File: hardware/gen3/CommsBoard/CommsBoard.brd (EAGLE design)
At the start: 140 x 107 mm, 41 parts, among them U1 ATMEGA165PV-8AU

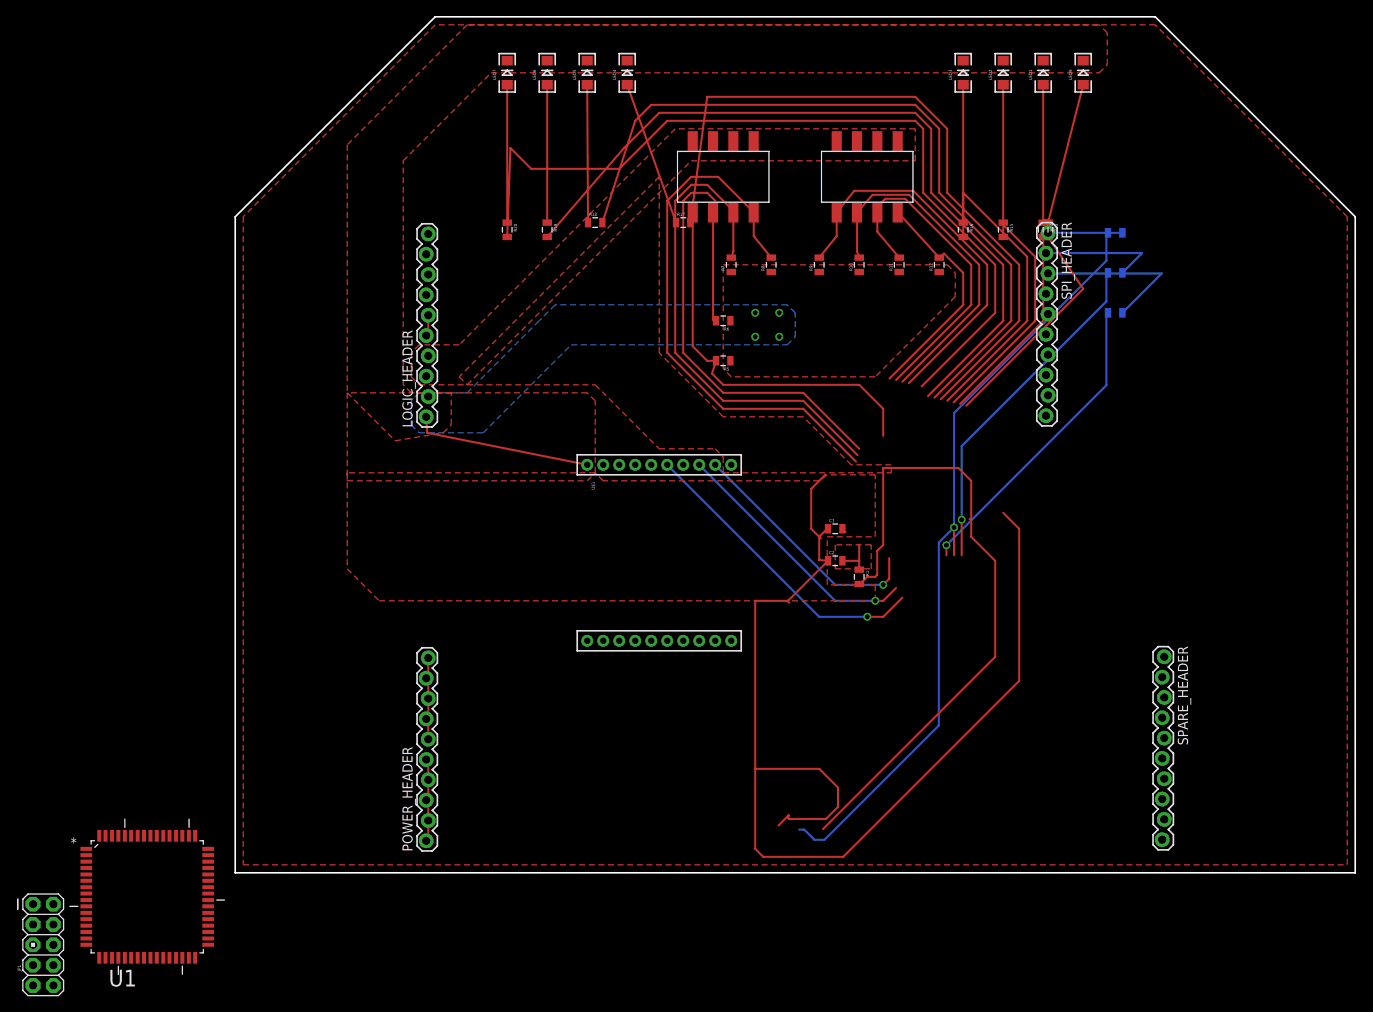
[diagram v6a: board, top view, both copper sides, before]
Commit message: new dimensions for boards
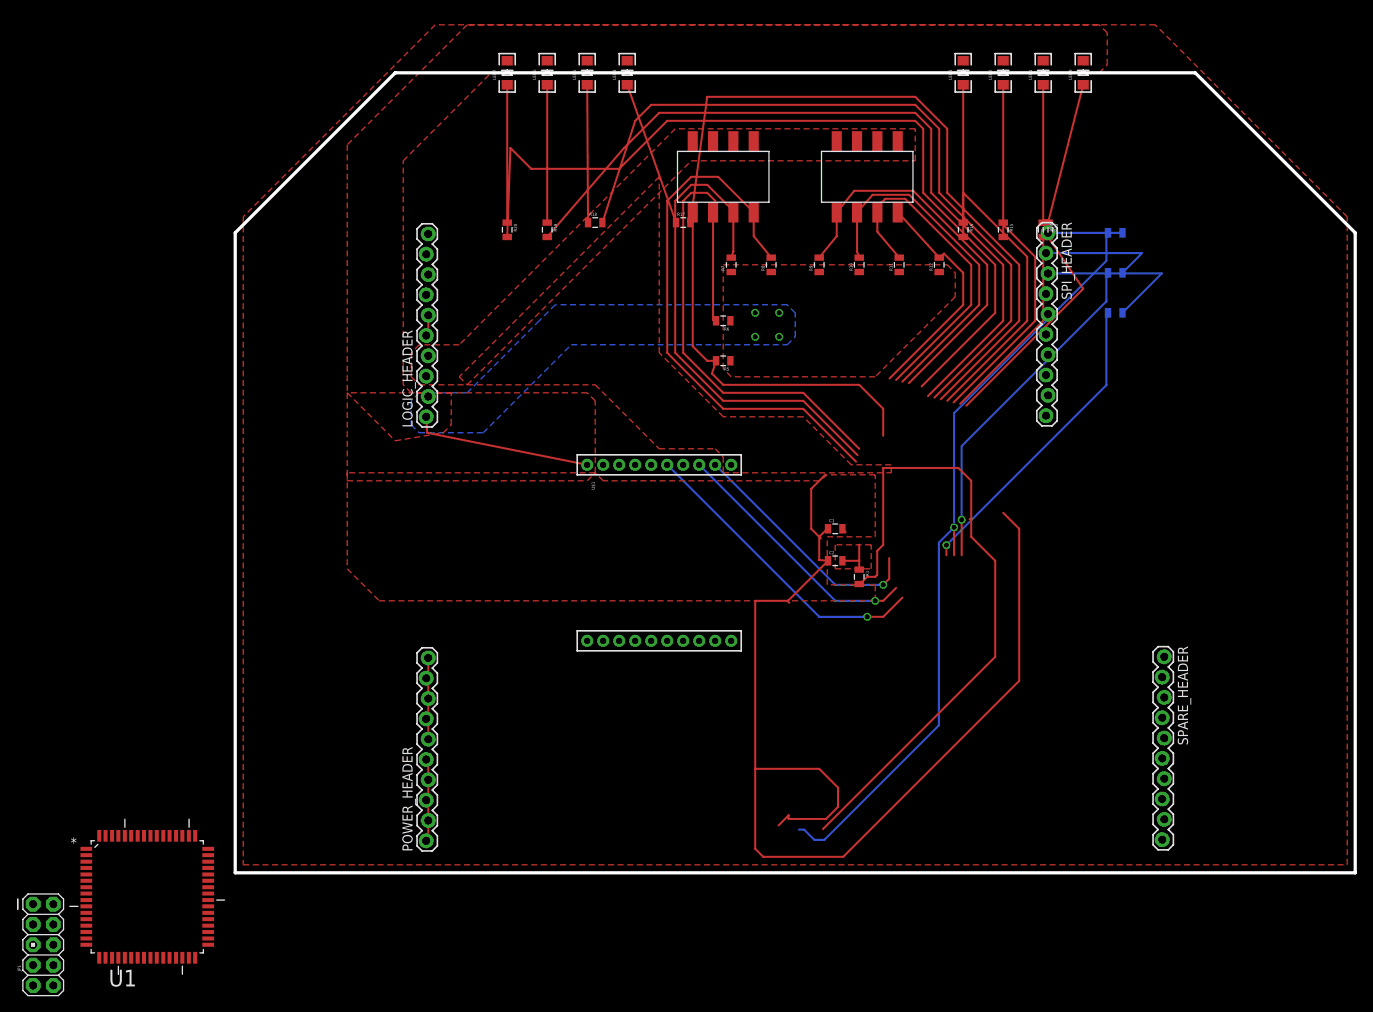
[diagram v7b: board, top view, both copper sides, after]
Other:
- board size 140 x 107 mm -> 140 x 100 mm
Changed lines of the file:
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@@
 <?xml version="1.0" encoding="utf-8"?>
 <!DOCTYPE eagle SYSTEM "eagle.dtd">
-<eagle version="7.2.0">
+<eagle version="6.4">
 <drawing>
 <settings>
@@
 <setting verticaltext="up"/>
 </settings>
-<grid distance="0.05" unitdist="inch" unit="inch" style="lines" multiple="1" display="yes" altdistance="0.01" altunitdist="mm" altunit="mm"/>
+<grid distance="1" unitdist="mm" unit="mm" style="lines" multiple="1" display="yes" altdistance="0.01" altunitdist="mm" altunit="mm"/>
 <layers>
 <layer number="1" name="Top" color="4" fill="1" visible="yes" active="yes"/>
@@
 <board>
 <plain>
-<wire x1="0" y1="0" x2="0" y2="82" width="0.2032" layer="20"/>
-<wire x1="0" y1="82" x2="25" y2="107" width="0.2032" layer="20"/>
-<wire x1="25" y1="107" x2="115" y2="107" width="0.2032" layer="20"/>
-<wire x1="115" y1="107" x2="140" y2="82" width="0.2032" layer="20"/>
-<wire x1="140" y1="82" x2="140" y2="0" width="0.2032" layer="20"/>
-<wire x1="140" y1="0" x2="0" y2="0" width="0.2032" layer="20"/>
-<wire x1="70" y1="107" x2="70" y2="0" width="0.4064" layer="23"/>
-<wire x1="120" y1="107" x2="120" y2="0" width="0.4064" layer="23"/>
-<wire x1="20" y1="0" x2="20" y2="107" width="0.4064" layer="23"/>
-<wire x1="-1" y1="82" x2="142" y2="82" width="0.4064" layer="23"/>
+<wire x1="0" y1="0" x2="0" y2="80" width="0.4064" layer="20"/>
+<wire x1="0" y1="80" x2="20" y2="100" width="0.4064" layer="20"/>
+<wire x1="20" y1="100" x2="120" y2="100" width="0.4064" layer="20"/>
+<wire x1="120" y1="100" x2="140" y2="80" width="0.4064" layer="20"/>
+<wire x1="140" y1="80" x2="140" y2="0" width="0.4064" layer="20"/>
+<wire x1="140" y1="0" x2="0" y2="0" width="0.4064" layer="20"/>
 </plain>
 <attributes>
@@
 <pass name="Default">
 <param name="RoutingGrid" value="12.5mil"/>
-<param name="AutoGrid" value="1"/>
-<param name="Efforts" value="0"/>
-<param name="TopRouterVariant" value="1"/>
 <param name="tpViaShape" value="round"/>
 <param name="PrefDir.1" value="*"/>

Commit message: headers placed
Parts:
- moved LOGIC_HEADER 40.0 mm to (23.0, 97.0), turned to 0 degrees
- moved SPARE_HEADER 32.6 mm to (94.0, 3.00), turned to 0 degrees
- moved SPI_HEADER 18.6 mm to (94.0, 97.0), turned to 0 degrees
- moved POWER_HEADER 1.41 mm to (23.0, 3.00), turned to 0 degrees
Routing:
- net GND: track 166.8 -> 0.00 mm, vias 4 -> 0
- net RLED4: track 106.4 -> 0.00 mm
- net MOSI: track 97.7 -> 0.00 mm, vias 1 -> 0
- net GLED4: track 96.8 -> 0.00 mm
- net RLED3: track 94.7 -> 0.00 mm
- net GLED3: track 89.1 -> 0.00 mm
- net 3.3V: track 82.0 -> 0.00 mm
- net BID0: track 68.6 -> 0.00 mm
- net BID2: track 66.2 -> 0.00 mm
- net BID1: track 62.4 -> 0.00 mm
- net EX3: track 49.2 -> 0.00 mm
- net BID3: track 48.7 -> 0.00 mm
- net EX2: track 44.2 -> 0.00 mm
- net MISO: track 42.9 -> 0.00 mm, vias 1 -> 0
- net EX1: track 42.0 -> 0.00 mm
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- removed copper zone on layer 1, net 3.3V
- removed copper zone on layer 1, net FILT
- removed copper zone on layer 1, net GND
- removed copper zone on layer 16, net GND
